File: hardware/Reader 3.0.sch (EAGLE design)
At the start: 10 parts, among them U1 ESP32-DEVKITC-32DHEADERS_ONLY

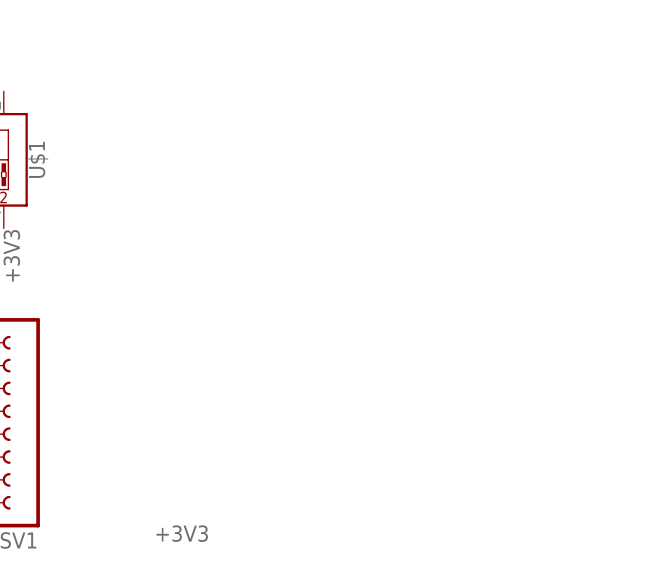
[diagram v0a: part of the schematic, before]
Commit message: add rj45 jack to board
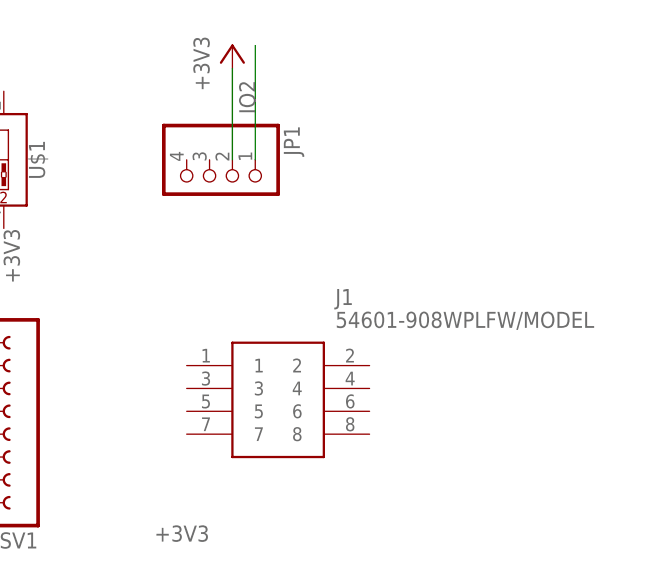
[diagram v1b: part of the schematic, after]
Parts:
- added J1: 54601-908WPLFW/MODEL, mcp:54601-908WPLFW/MODEL
- added JP1: (no value), mcp:PINHD-1X4/90
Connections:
- net +3V3: now also JP1.2
- net IO2: now also JP1.1

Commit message: Assign jack pins
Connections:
- new net +5V: J1.1, J1.5, U1.EXT_5V
- new net N$10: J1.6
- new net N$7: J1.2
- new net N$8: J1.7
- net GND: now also J1.4, J1.8
- net RELAY_OUT: now also J1.3, U1.IO33; no longer U1.IO23

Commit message: add current sense input
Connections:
- removed net N$8: J1.7
- new net CURRENT_IN: J1.7, U1.IO25
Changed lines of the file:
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@@
 <pinref part="U1" gate="G$1" pin="IO33"/>
 <wire x1="43.18" y1="48.26" x2="33.02" y2="48.26" width="0.1524" layer="91"/>
+<label x="30.48" y="48.26" size="1.778" layer="95"/>
 </segment>
 </net>
@@
 </segment>
 </net>
-<net name="N$8" class="0">
-<segment>
-<pinref part="J1" gate="G$1" pin="7"/>
-<wire x1="162.56" y1="27.94" x2="154.94" y2="27.94" width="0.1524" layer="91"/>
-</segment>
-</net>
 <net name="+5V" class="0">
 <segment>
@@
 </segment>
 </net>
+<net name="CURRENT_IN" class="0">
+<segment>
+<pinref part="U1" gate="G$1" pin="IO25"/>
+<wire x1="43.18" y1="45.72" x2="33.02" y2="45.72" width="0.1524" layer="91"/>
+<label x="30.48" y="45.72" size="1.778" layer="95"/>
+</segment>
+<segment>
+<pinref part="J1" gate="G$1" pin="7"/>
+<wire x1="162.56" y1="27.94" x2="154.94" y2="27.94" width="0.1524" layer="91"/>
+<label x="149.86" y="27.94" size="1.778" layer="95"/>
+</segment>
+</net>

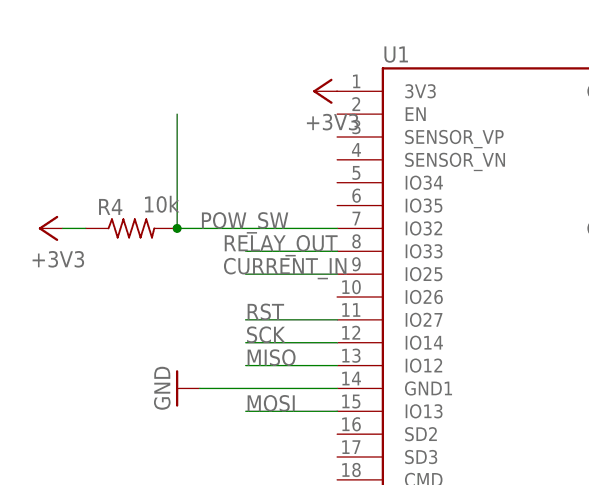
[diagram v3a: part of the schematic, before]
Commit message: Slight adjustments to board layout, add pullup resistor
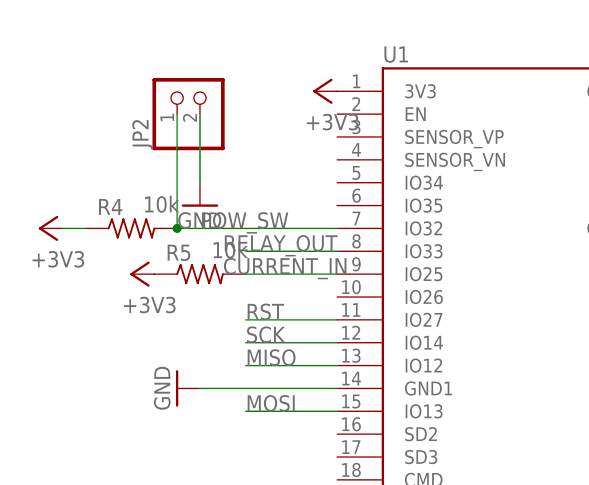
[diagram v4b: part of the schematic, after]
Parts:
- added JP2: (no value), mcp:PINHD-1X2/90
- added R5: 10k, mcp:R-US
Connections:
- net +3V3: now also R5.1
- net CURRENT_IN: now also R5.2
- net GND: now also JP2.2
- net POW_SW: now also JP2.1
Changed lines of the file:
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@@
 </layers>
 <schematic xreflabel="%F%N/%S.%C%R" xrefpart="/%S.%C%R">
+<fusionteam huburn="a.cGVyc29uYWw6dWUyOTczZTRi" projecturn="a.cGVyc29uYWw6dWUyOTczZTRiIzIwMTcxMTEwMTAzMzQ5ODMx" folderUrn="urn:adsk.wipprod:fs.folder:co.dl1-tHgaQOq5uV8proHg1w" urn="urn:adsk.wipprod:dm.lineage:S571tyeVR5u6rjlXeDXGWw"  versionUrn="urn:adsk.wipprod:fs.file:vf.S571tyeVR5u6rjlXeDXGWw?version=1" camFileUrn="" camFileVersionUrn="" lastpublishedchangeguid="ce8bdec3-a423-5e08-8694-282247e0b63f"/>
 <attributes>
 </attributes>
@@
 <part name="P+2" library="supply1" library_urn="urn:adsk.eagle:library:371" deviceset="+5V" device=""/>
 <part name="P+3" library="supply1" library_urn="urn:adsk.eagle:library:371" deviceset="+5V" device=""/>
+<part name="JP2" library="mcp" library_urn="urn:adsk.eagle:library:9418757" deviceset="PINHD-1X2" device="/90" package3d_urn="urn:adsk.eagle:package:22437/2"/>
+<part name="GND8" library="supply1" library_urn="urn:adsk.eagle:library:371" deviceset="GND" device=""/>
+<part name="R5" library="mcp" library_urn="urn:adsk.eagle:library:9418757" deviceset="R-US" device="" package3d_urn="urn:adsk.eagle:package:23498/2" value="10k"/>
+<part name="+3V6" library="supply1" library_urn="urn:adsk.eagle:library:371" deviceset="+3V3" device=""/>
 </parts>
 <sheets>
@@
 <attribute name="VALUE" x="45.72" y="17.78" size="1.778" layer="96" rot="R180"/>
 </instance>
+<instance part="JP2" gate="G$1" x="27.94" y="66.04" smashed="yes" rot="R90">
+<attribute name="NAME" x="22.225" y="59.69" size="1.778" layer="95" rot="R90"/>
+<attribute name="VALUE" x="33.02" y="59.69" size="1.778" layer="96" rot="R90"/>
+</instance>
+<instance part="GND8" gate="1" x="27.94" y="53.34" smashed="yes">
+<attribute name="VALUE" x="25.4" y="50.8" size="1.778" layer="96"/>
+</instance>
+<instance part="R5" gate="G$1" x="27.94" y="45.72" smashed="yes">
+<attribute name="NAME" x="24.13" y="47.2186" size="1.778" layer="95"/>
+<attribute name="VALUE" x="29.21" y="47.498" size="1.778" layer="96"/>
+</instance>
+<instance part="+3V6" gate="G$1" x="20.32" y="45.72" smashed="yes" rot="R90">
+<attribute name="VALUE" x="25.4" y="43.18" size="1.778" layer="96" rot="R180"/>
+</instance>
 </instances>
 <busses>
@@
 <pinref part="GND7" gate="1" pin="GND"/>
 </segment>
+<segment>
+<pinref part="JP2" gate="G$1" pin="2"/>
+<wire x1="27.94" y1="63.5" x2="27.94" y2="55.88" width="0.1524" layer="91"/>
+<pinref part="GND8" gate="1" pin="GND"/>
+</segment>
 </net>
 <net name="+3V3" class="0">
@@
 <pinref part="+3V5" gate="G$1" pin="+3V3"/>
 <wire x1="167.64" y1="68.58" x2="167.64" y2="58.42" width="0.1524" layer="91"/>
+</segment>
+<segment>
+<pinref part="R5" gate="G$1" pin="1"/>
+<pinref part="+3V6" gate="G$1" pin="+3V3"/>
 </segment>
 </net>
@@
 <wire x1="25.4" y1="50.8" x2="25.4" y2="63.5" width="0.1524" layer="91"/>
 <junction x="25.4" y="50.8"/>
+<pinref part="JP2" gate="G$1" pin="1"/>
 </segment>
 </net>
@@
 <wire x1="43.18" y1="45.72" x2="33.02" y2="45.72" width="0.1524" layer="91"/>
 <label x="30.48" y="45.72" size="1.778" layer="95"/>
-</segment>
-<segment>
+<pinref part="R5" gate="G$1" pin="2"/>
+</segment>
+<segment>

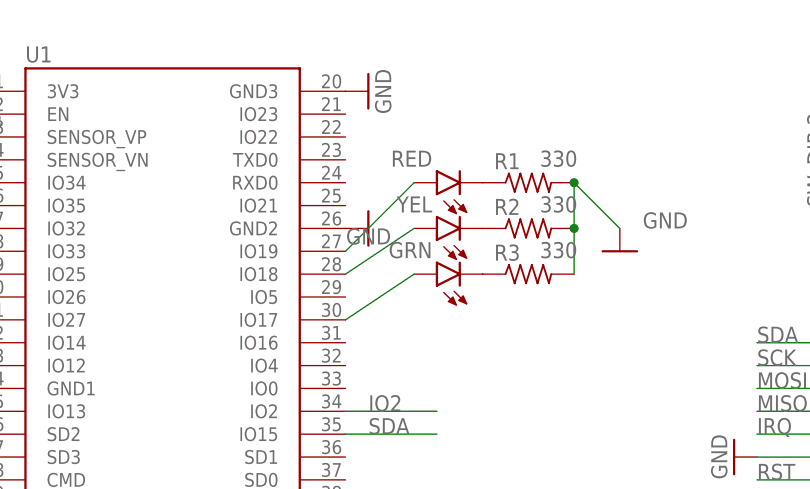
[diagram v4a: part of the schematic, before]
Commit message: change LED names in circuit layout
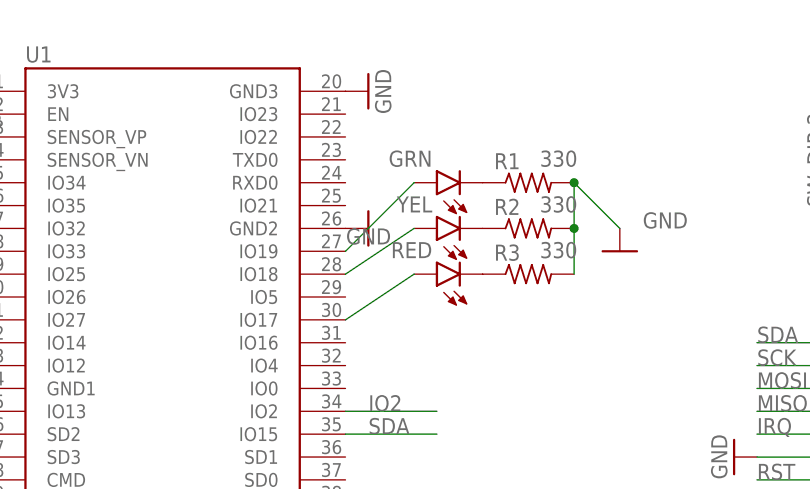
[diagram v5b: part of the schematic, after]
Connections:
- net N$1: now also RED.A; no longer GRN.A
- net N$3: now also GRN.A; no longer RED.A
- net N$4: now also GRN.C; no longer RED.C
- net N$6: now also RED.C; no longer GRN.C
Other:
- moved on the sheet: GRN, RED
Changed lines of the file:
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@@
 <part name="+3V1" library="supply1" library_urn="urn:adsk.eagle:library:371" deviceset="+3V3" device=""/>
 <part name="+3V2" library="supply1" library_urn="urn:adsk.eagle:library:371" deviceset="+3V3" device=""/>
+<part name="RED" library="led" library_urn="urn:adsk.eagle:library:259" deviceset="LED" device="5MM" package3d_urn="urn:adsk.eagle:package:15799/2"/>
+<part name="YEL" library="led" library_urn="urn:adsk.eagle:library:259" deviceset="LED" device="5MM" package3d_urn="urn:adsk.eagle:package:15799/2"/>
 <part name="GRN" library="led" library_urn="urn:adsk.eagle:library:259" deviceset="LED" device="5MM" package3d_urn="urn:adsk.eagle:package:15799/2"/>
-<part name="YEL" library="led" library_urn="urn:adsk.eagle:library:259" deviceset="LED" device="5MM" package3d_urn="urn:adsk.eagle:package:15799/2"/>
-<part name="RED" library="led" library_urn="urn:adsk.eagle:library:259" deviceset="LED" device="5MM" package3d_urn="urn:adsk.eagle:package:15799/2"/>
 <part name="R1" library="mcp" library_urn="urn:adsk.eagle:library:9418757" deviceset="R-US" device="" package3d_urn="urn:adsk.eagle:package:23498/2" value="330"/>
 <part name="R2" library="mcp" library_urn="urn:adsk.eagle:library:9418757" deviceset="R-US" device="" package3d_urn="urn:adsk.eagle:package:23498/2" value="330"/>
@@
 <attribute name="VALUE" x="127" y="17.78" size="1.778" layer="96" rot="R180"/>
 </instance>
-<instance part="GRN" gate="G$1" x="93.98" y="45.72" smashed="yes" rot="R90">
+<instance part="RED" gate="G$1" x="93.98" y="45.72" smashed="yes" rot="R90">
 <attribute name="NAME" x="93.472" y="49.276" size="1.778" layer="95" rot="R180"/>
 <attribute name="VALUE" x="98.552" y="51.435" size="1.778" layer="96" rot="R180"/>
@@
 <attribute name="VALUE" x="98.552" y="56.515" size="1.778" layer="96" rot="R180"/>
 </instance>
-<instance part="RED" gate="G$1" x="93.98" y="55.88" smashed="yes" rot="R90">
+<instance part="GRN" gate="G$1" x="93.98" y="55.88" smashed="yes" rot="R90">
 <attribute name="NAME" x="93.472" y="59.436" size="1.778" layer="95" rot="R180"/>
 <attribute name="VALUE" x="98.552" y="61.595" size="1.778" layer="96" rot="R180"/>
@@
 <segment>
 <pinref part="U1" gate="G$1" pin="IO17"/>
-<pinref part="GRN" gate="G$1" pin="A"/>
+<pinref part="RED" gate="G$1" pin="A"/>
 <wire x1="91.44" y1="45.72" x2="83.82" y2="40.64" width="0.1524" layer="91"/>
 </segment>
@@
 <segment>
 <pinref part="U1" gate="G$1" pin="IO19"/>
-<pinref part="RED" gate="G$1" pin="A"/>
+<pinref part="GRN" gate="G$1" pin="A"/>
 <wire x1="91.44" y1="55.88" x2="83.82" y2="48.26" width="0.1524" layer="91"/>
 </segment>
@@
 <net name="N$4" class="0">
 <segment>
-<pinref part="RED" gate="G$1" pin="C"/>
+<pinref part="GRN" gate="G$1" pin="C"/>
 <pinref part="R1" gate="G$1" pin="1"/>
 </segment>
@@
 <net name="N$6" class="0">
 <segment>
-<pinref part="GRN" gate="G$1" pin="C"/>
+<pinref part="RED" gate="G$1" pin="C"/>
 <pinref part="R3" gate="G$1" pin="1"/>
 </segment>

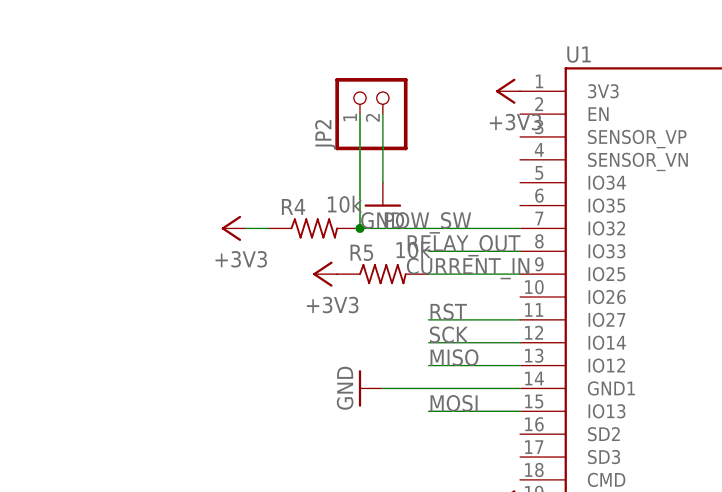
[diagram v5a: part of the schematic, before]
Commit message: fix current input wiring   * ADC2 on IO25 is not usable when WiFi is active.   * switch to ADC1 on IO32   * add capacitor to input   * remove pullup resistor
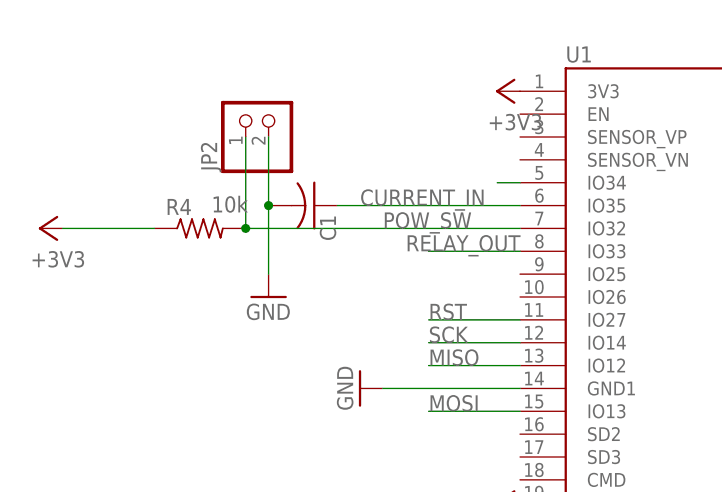
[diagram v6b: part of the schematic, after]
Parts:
- removed R5: 10k, mcp:R-US
- added C1: (no value), rcl:C-US025-025X050
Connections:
- new net N$8: U1.IO34
- net +3V3: no longer R5.1
- net CURRENT_IN: now also C1.1, U1.IO35; no longer R5.2, U1.IO25
- net GND: now also C1.2
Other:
- moved on the sheet: JP2, R4
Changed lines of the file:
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@@
 <part name="JP2" library="mcp" library_urn="urn:adsk.eagle:library:9418757" deviceset="PINHD-1X2" device="/90" package3d_urn="urn:adsk.eagle:package:22437/2"/>
 <part name="GND8" library="supply1" library_urn="urn:adsk.eagle:library:371" deviceset="GND" device=""/>
-<part name="R5" library="mcp" library_urn="urn:adsk.eagle:library:9418757" deviceset="R-US" device="" package3d_urn="urn:adsk.eagle:package:23498/2" value="10k"/>
-<part name="+3V6" library="supply1" library_urn="urn:adsk.eagle:library:371" deviceset="+3V3" device=""/>
+<part name="C1" library="rcl" library_urn="urn:adsk.eagle:library:334" deviceset="C-US" device="025-025X050" package3d_urn="urn:adsk.eagle:package:23629/2"/>
 </parts>
 <sheets>
@@
 <attribute name="VALUE" x="142.24" y="50.8" size="1.778" layer="96" rot="R270"/>
 </instance>
-<instance part="R4" gate="G$1" x="20.32" y="50.8" smashed="yes">
-<attribute name="NAME" x="16.51" y="52.2986" size="1.778" layer="95"/>
-<attribute name="VALUE" x="21.59" y="52.578" size="1.778" layer="96"/>
-</instance>
-<instance part="+3V4" gate="G$1" x="10.16" y="50.8" smashed="yes" rot="R90">
-<attribute name="VALUE" x="15.24" y="48.26" size="1.778" layer="96" rot="R180"/>
+<instance part="R4" gate="G$1" x="7.62" y="50.8" smashed="yes">
+<attribute name="NAME" x="3.81" y="52.2986" size="1.778" layer="95"/>
+<attribute name="VALUE" x="8.89" y="52.578" size="1.778" layer="96"/>
+</instance>
+<instance part="+3V4" gate="G$1" x="-10.16" y="50.8" smashed="yes" rot="R90">
+<attribute name="VALUE" x="-5.08" y="48.26" size="1.778" layer="96" rot="R180"/>
 </instance>
 <instance part="U$1" gate="G$1" x="142.24" y="58.42" smashed="yes" rot="R270">
@@
 <attribute name="VALUE" x="45.72" y="17.78" size="1.778" layer="96" rot="R180"/>
 </instance>
-<instance part="JP2" gate="G$1" x="27.94" y="66.04" smashed="yes" rot="R90">
-<attribute name="NAME" x="22.225" y="59.69" size="1.778" layer="95" rot="R90"/>
-<attribute name="VALUE" x="33.02" y="59.69" size="1.778" layer="96" rot="R90"/>
-</instance>
-<instance part="GND8" gate="1" x="27.94" y="53.34" smashed="yes">
-<attribute name="VALUE" x="25.4" y="50.8" size="1.778" layer="96"/>
-</instance>
-<instance part="R5" gate="G$1" x="27.94" y="45.72" smashed="yes">
-<attribute name="NAME" x="24.13" y="47.2186" size="1.778" layer="95"/>
-<attribute name="VALUE" x="29.21" y="47.498" size="1.778" layer="96"/>
-</instance>
-<instance part="+3V6" gate="G$1" x="20.32" y="45.72" smashed="yes" rot="R90">
-<attribute name="VALUE" x="25.4" y="43.18" size="1.778" layer="96" rot="R180"/>
+<instance part="JP2" gate="G$1" x="15.24" y="63.5" smashed="yes" rot="R90">
+<attribute name="NAME" x="9.525" y="57.15" size="1.778" layer="95" rot="R90"/>
+<attribute name="VALUE" x="20.32" y="57.15" size="1.778" layer="96" rot="R90"/>
+</instance>
+<instance part="GND8" gate="1" x="15.24" y="43.18" smashed="yes">
+<attribute name="VALUE" x="12.7" y="40.64" size="1.778" layer="96"/>
+</instance>
+<instance part="C1" gate="G$1" x="20.32" y="53.34" smashed="yes" rot="R270">
+<attribute name="NAME" x="20.955" y="52.324" size="1.778" layer="95" rot="R270"/>
+<attribute name="VALUE" x="16.129" y="52.324" size="1.778" layer="96" rot="R270"/>
 </instance>
 </instances>
@@
 <segment>
 <pinref part="JP2" gate="G$1" pin="2"/>
-<wire x1="27.94" y1="63.5" x2="27.94" y2="55.88" width="0.1524" layer="91"/>
+<wire x1="15.24" y1="60.96" x2="15.24" y2="53.34" width="0.1524" layer="91"/>
 <pinref part="GND8" gate="1" pin="GND"/>
+<pinref part="C1" gate="G$1" pin="2"/>
+<wire x1="15.24" y1="53.34" x2="15.24" y2="45.72" width="0.1524" layer="91"/>
+<junction x="15.24" y="53.34"/>
 </segment>
 </net>
@@
 <pinref part="R4" gate="G$1" pin="1"/>
 <pinref part="+3V4" gate="G$1" pin="+3V3"/>
-<wire x1="12.7" y1="50.8" x2="15.24" y2="50.8" width="0.1524" layer="91"/>
+<wire x1="-7.62" y1="50.8" x2="2.54" y2="50.8" width="0.1524" layer="91"/>
 </segment>
 <segment>
@@
 <wire x1="167.64" y1="68.58" x2="167.64" y2="58.42" width="0.1524" layer="91"/>
 </segment>
-<segment>
-<pinref part="R5" gate="G$1" pin="1"/>
-<pinref part="+3V6" gate="G$1" pin="+3V3"/>
-</segment>
 </net>
 <net name="N$1" class="0">
@@
 <pinref part="U1" gate="G$1" pin="IO32"/>
 <pinref part="R4" gate="G$1" pin="2"/>
-<wire x1="25.4" y1="50.8" x2="43.18" y2="50.8" width="0.1524" layer="91"/>
+<wire x1="12.7" y1="50.8" x2="43.18" y2="50.8" width="0.1524" layer="91"/>
 <label x="27.94" y="50.8" size="1.778" layer="95"/>
-<wire x1="25.4" y1="50.8" x2="25.4" y2="63.5" width="0.1524" layer="91"/>
-<junction x="25.4" y="50.8"/>
+<wire x1="12.7" y1="50.8" x2="12.7" y2="60.96" width="0.1524" layer="91"/>
+<junction x="12.7" y="50.8"/>
 <pinref part="JP2" gate="G$1" pin="1"/>
 </segment>
@@
 <net name="CURRENT_IN" class="0">
 <segment>
-<pinref part="U1" gate="G$1" pin="IO25"/>
-<wire x1="43.18" y1="45.72" x2="33.02" y2="45.72" width="0.1524" layer="91"/>
-<label x="30.48" y="45.72" size="1.778" layer="95"/>
-<pinref part="R5" gate="G$1" pin="2"/>
-</segment>
-<segment>
 <pinref part="J1" gate="G$1" pin="7"/>
 <wire x1="162.56" y1="27.94" x2="154.94" y2="27.94" width="0.1524" layer="91"/>
 <label x="149.86" y="27.94" size="1.778" layer="95"/>
+</segment>
+<segment>
+<pinref part="U1" gate="G$1" pin="IO35"/>
+<wire x1="43.18" y1="53.34" x2="22.86" y2="53.34" width="0.1524" layer="91"/>
+<pinref part="C1" gate="G$1" pin="1"/>
+<label x="25.4" y="53.34" size="1.778" layer="95"/>
+</segment>
+</net>
+<net name="N$8" class="0">
+<segment>
+<pinref part="U1" gate="G$1" pin="IO34"/>
+<wire x1="40.64" y1="55.88" x2="43.18" y2="55.88" width="0.1524" layer="91"/>
 </segment>
 </net>
@@
 packages will not be understood (or retained) with this version.
 </note>
+<note version="8.4" severity="warning">
+Since Version 8.4, EAGLE supports properties for SPICE simulation.
+Probes in schematics and SPICE mapping objects found in parts and library devices
+will not be understood with this version. Update EAGLE to the latest version
+for full support of SPICE simulation.
+</note>
 </compatibility>
